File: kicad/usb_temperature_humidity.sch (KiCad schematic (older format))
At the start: 10 parts, among them SW1 SW_SPDT, SW2 SW_SPDT, U1 SeeeduinoXIAO, U2 SHT-31, U3 PinHeader_XIAO, U4 PinHeader_XIAO

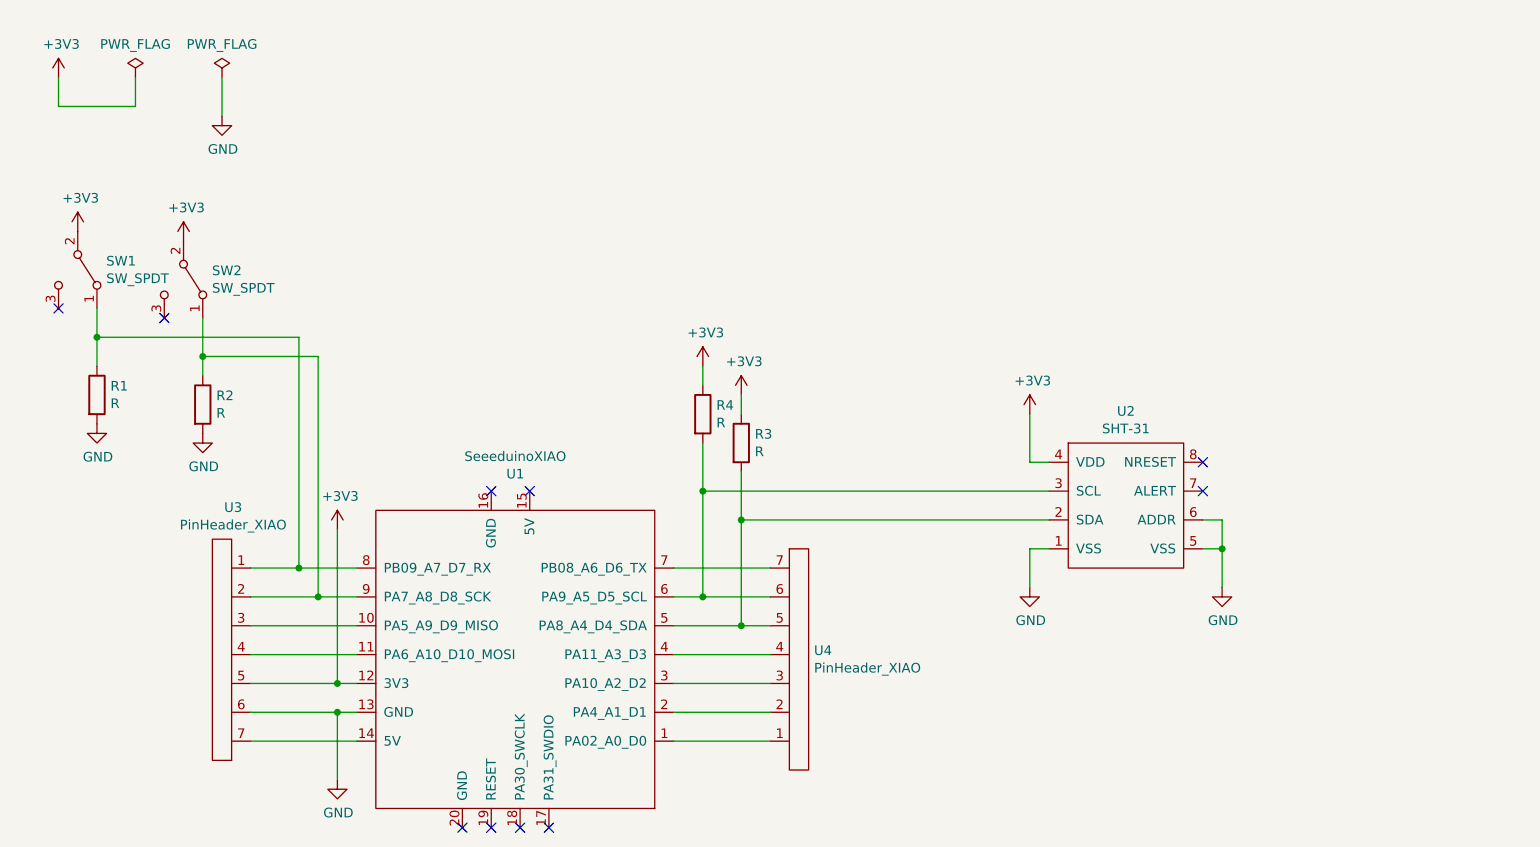
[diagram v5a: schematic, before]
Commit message: OPENジャンパを介してALERT,NRESETをXIAOに繋いだ
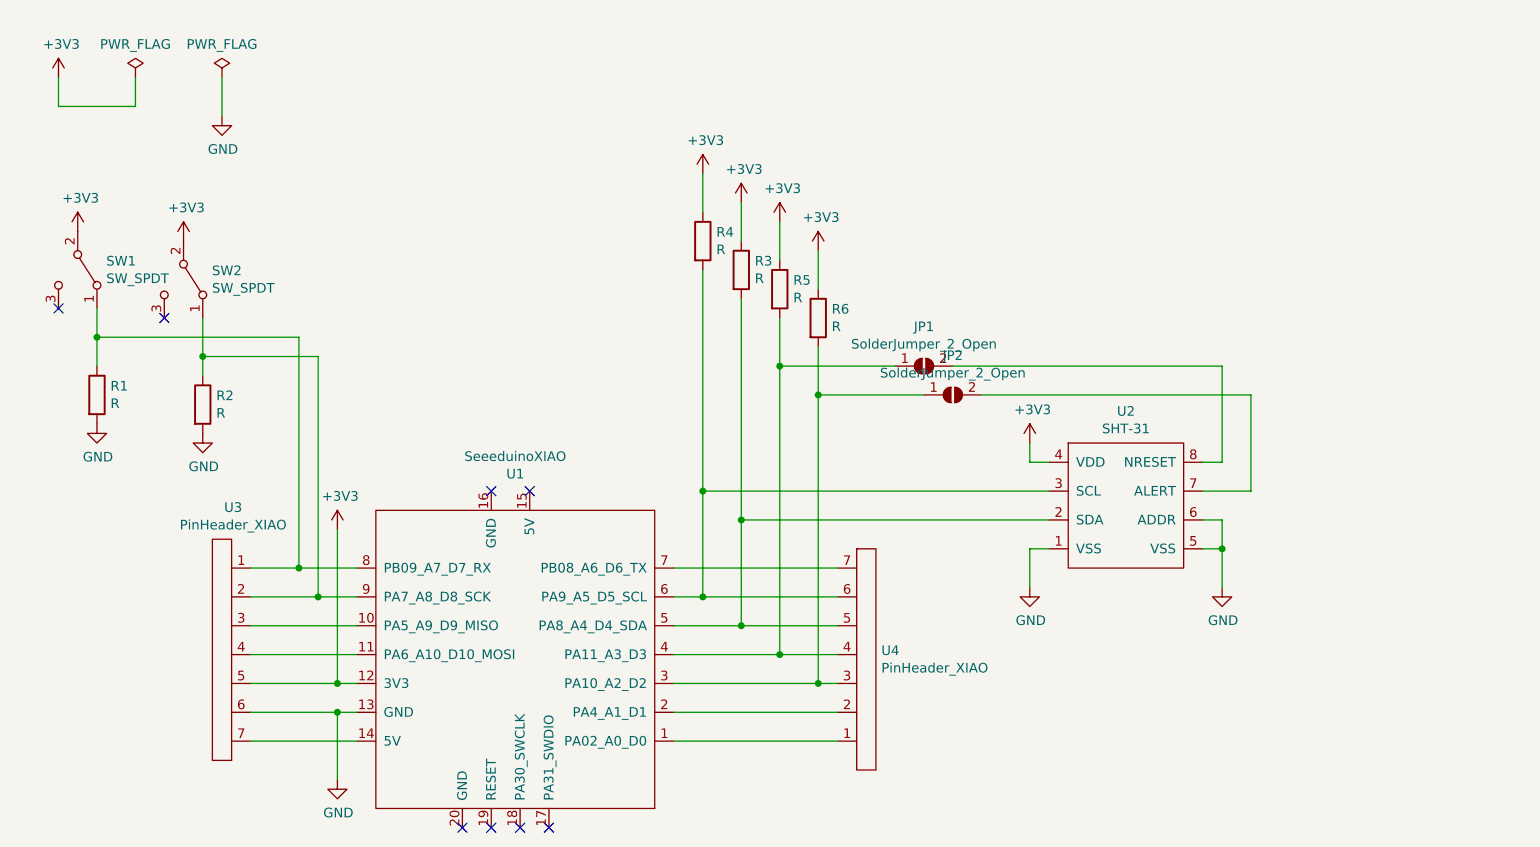
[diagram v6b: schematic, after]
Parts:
- added JP1, JP2: SolderJumper_2_Open, Jumper:SolderJumper-2_P1.3mm_Open_TrianglePad1.0x1.5mm, symbol Jumper:SolderJumper_2_Open
- added R5, R6: R, Resistor_THT:R_Axial_DIN0207_L6.3mm_D2.5mm_P10.16mm_Horizontal, symbol Device:R
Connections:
- net +3V3: now also R5.1, R6.1
- net at U1.3 (PA10_A2_D2), U4.3: now also JP2.1 (A), R6.2
- net at U1.4 (PA11_A3_D3), U4.4: now also JP1.1 (A), R5.2
- net at U2.7 (ALERT): now also JP2.2 (B)
- net at U2.8 (NRESET): now also JP1.2 (B)
- no-connect marks 10 -> 8
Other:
- moved on the sheet: R3, R4, U4
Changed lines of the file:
@@
 	900  1050 900  1200
-$Comp
-L power:+3V3 #PWR03
-U 1 1 5F4047C9
-P 2350 3400
-F 0 "#PWR03" H 2350 3250 50  0001 C CNN
-F 1 "+3V3" H 2365 3573 50  0000 C CNN
-F 2 "" H 2350 3400 50  0001 C CNN
-F 3 "" H 2350 3400 50  0001 C CNN
-	1    2350 3400
-	1    0    0    -1
-$EndComp
 $Comp
 L power:GND #PWR02
@@
 L Device:R R4
 U 1 1 5F3FC51D
-P 4250 2800
-F 0 "R4" H 4320 2846 50  0000 L CNN
-F 1 "R" H 4320 2755 50  0000 L CNN
-F 2 "Resistor_THT:R_Axial_DIN0207_L6.3mm_D2.5mm_P10.16mm_Horizontal" V 4180 2800 50  0001 C CNN
-F 3 "~" H 4250 2800 50  0001 C CNN
-	1    4250 2800
+P 4250 1900
+F 0 "R4" H 4320 1946 50  0000 L CNN
+F 1 "R" H 4320 1855 50  0000 L CNN
+F 2 "Resistor_THT:R_Axial_DIN0207_L6.3mm_D2.5mm_P10.16mm_Horizontal" V 4180 1900 50  0001 C CNN
+F 3 "~" H 4250 1900 50  0001 C CNN
+	1    4250 1900
 	1    0    0    -1
 $EndComp
@@
 L Device:R R3
 U 1 1 5F3FC106
-P 4450 2950
-F 0 "R3" H 4520 2996 50  0000 L CNN
-F 1 "R" H 4520 2905 50  0000 L CNN
-F 2 "Resistor_THT:R_Axial_DIN0207_L6.3mm_D2.5mm_P10.16mm_Horizontal" V 4380 2950 50  0001 C CNN
-F 3 "~" H 4450 2950 50  0001 C CNN
-	1    4450 2950
+P 4450 2050
+F 0 "R3" H 4520 2096 50  0000 L CNN
+F 1 "R" H 4520 2005 50  0000 L CNN
+F 2 "Resistor_THT:R_Axial_DIN0207_L6.3mm_D2.5mm_P10.16mm_Horizontal" V 4380 2050 50  0001 C CNN
+F 3 "~" H 4450 2050 50  0001 C CNN
+	1    4450 2050
 	1    0    0    -1
 $EndComp
@@
 $EndComp
 Wire Wire Line
-	4250 2950 4250 3200
-Wire Wire Line
-	4450 3100 4450 3350
-Wire Wire Line
 	6050 3200 4250 3200
-Connection ~ 4250 3200
-Wire Wire Line
-	4250 3200 4250 3750
 Wire Wire Line
 	6050 3350 4450 3350
-Connection ~ 4450 3350
 Wire Wire Line
 	4450 3350 4450 3900
@@
 Wire Wire Line
 	6050 3050 5950 3050
-Wire Wire Line
-	5950 3050 5950 2800
-NoConn ~ 6850 3050
-NoConn ~ 6850 3200
 NoConn ~ 3350 3200
 NoConn ~ 3150 3200
@@
 NoConn ~ 3150 4950
 NoConn ~ 3000 4950
-$Comp
-L power:+3V3 #PWR06
-U 1 1 5F3FB873
-P 4450 2700
-F 0 "#PWR06" H 4450 2550 50  0001 C CNN
-F 1 "+3V3" H 4465 2873 50  0000 C CNN
-F 2 "" H 4450 2700 50  0001 C CNN
-F 3 "" H 4450 2700 50  0001 C CNN
-	1    4450 2700
-	1    0    0    -1
-$EndComp
-$Comp
-L power:+3V3 #PWR05
-U 1 1 5F3FBC68
-P 4250 2550
-F 0 "#PWR05" H 4250 2400 50  0001 C CNN
-F 1 "+3V3" H 4265 2723 50  0000 C CNN
-F 2 "" H 4250 2550 50  0001 C CNN
-F 3 "" H 4250 2550 50  0001 C CNN
-	1    4250 2550
-	1    0    0    -1
-$EndComp
-Wire Wire Line
-	4250 2550 4250 2650
-Wire Wire Line
-	4450 2700 4450 2800
 Wire Wire Line
 	1750 1050 1750 1250
@@
 L power:+3V3 #PWR07
 U 1 1 5F40C82C
-P 5950 2800
-F 0 "#PWR07" H 5950 2650 50  0001 C CNN
-F 1 "+3V3" H 5965 2973 50  0000 C CNN
-F 2 "" H 5950 2800 50  0001 C CNN
-F 3 "" H 5950 2800 50  0001 C CNN
-	1    5950 2800
+P 5950 2950
+F 0 "#PWR07" H 5950 2800 50  0001 C CNN
+F 1 "+3V3" H 5965 3123 50  0000 C CNN
+F 2 "" H 5950 2950 50  0001 C CNN
+F 3 "" H 5950 2950 50  0001 C CNN
+	1    5950 2950
 	1    0    0    -1
 $EndComp
@@
 NoConn ~ 900  2250
 $Comp
-L kicad_mylib:SHT-31 U2
-U 1 1 5FB3D220
-P 6150 3600
-F 0 "U2" H 6450 4415 50  0000 C CNN
-F 1 "SHT-31" H 6450 4324 50  0000 C CNN
-F 2 "kicad_mylib:SHT-31" H 6700 4300 50  0001 C CNN
-F 3 "" H 6700 4300 50  0001 C CNN
-	1    6150 3600
-	1    0    0    -1
-$EndComp
-$Comp
 L power:GND #PWR013
 U 1 1 5FB42E84
@@
 L kicad_mylib:PinHeader_XIAO U4
 U 1 1 5FB5C045
-P 4700 4650
-F 0 "U4" H 4828 5271 50  0000 L CNN
-F 1 "PinHeader_XIAO" H 4828 5180 50  0000 L CNN
-F 2 "kicad_mylib:PinHeader_XIAO" H 4750 5900 50  0001 C CNN
-F 3 "" H 4750 5900 50  0001 C CNN
-	1    4700 4650
+P 5050 4650
+F 0 "U4" H 5178 5271 50  0000 L CNN
+F 1 "PinHeader_XIAO" H 5178 5180 50  0000 L CNN
+F 2 "kicad_mylib:PinHeader_XIAO" H 5100 5900 50  0001 C CNN
+F 3 "" H 5100 5900 50  0001 C CNN
+	1    5050 4650
 	1    0    0    -1
 $EndComp
@@
 	-1   0    0    1
 $EndComp
-Wire Wire Line
-	4600 4500 4100 4500
-Wire Wire Line
-	4600 4350 4100 4350
-Wire Wire Line
-	4600 4200 4100 4200
-Wire Wire Line
-	4100 4050 4600 4050
-Wire Wire Line
-	4600 3900 4450 3900
 Connection ~ 4450 3900
-Wire Wire Line
-	4600 3750 4250 3750
 Connection ~ 4250 3750
-Wire Wire Line
-	4100 3600 4600 3600
 Wire Wire Line
 	2150 3600 1900 3600
@@
 Wire Wire Line
 	1900 4500 2450 4500
+Wire Wire Line
+	4250 3750 4950 3750
+$Comp
+L Jumper:SolderJumper_2_Open JP1
+U 1 1 5FB82EA1
+P 5400 2550
+F 0 "JP1" H 5400 2755 50  0000 C CNN
+F 1 "SolderJumper_2_Open" H 5400 2664 50  0000 C CNN
+F 2 "Jumper:SolderJumper-2_P1.3mm_Open_TrianglePad1.0x1.5mm" H 5400 2550 50  0001 C CNN
+F 3 "~" H 5400 2550 50  0001 C CNN
+	1    5400 2550
+	1    0    0    -1
+$EndComp
+$Comp
+L Jumper:SolderJumper_2_Open JP2
+U 1 1 5FB83C68
+P 5550 2700
+F 0 "JP2" H 5550 2905 50  0000 C CNN
+F 1 "SolderJumper_2_Open" H 5550 2814 50  0000 C CNN
+F 2 "Jumper:SolderJumper-2_P1.3mm_Open_TrianglePad1.0x1.5mm" H 5550 2700 50  0001 C CNN
+F 3 "~" H 5550 2700 50  0001 C CNN
+	1    5550 2700
+	1    0    0    -1
+$EndComp
+Wire Wire Line
+	5950 2950 5950 3050
+Wire Wire Line
+	4100 4200 4850 4200
+$Comp
+L Device:R R6
+U 1 1 5FB80CC5
+P 4850 2300
+F 0 "R6" H 4920 2346 50  0000 L CNN
+F 1 "R" H 4920 2255 50  0000 L CNN
+F 2 "Resistor_THT:R_Axial_DIN0207_L6.3mm_D2.5mm_P10.16mm_Horizontal" V 4780 2300 50  0001 C CNN
+F 3 "~" H 4850 2300 50  0001 C CNN
+	1    4850 2300
+	1    0    0    -1
+$EndComp
+$Comp
+L Device:R R5
+U 1 1 5FB808DA
+P 4650 2150
+F 0 "R5" H 4720 2196 50  0000 L CNN
+F 1 "R" H 4720 2105 50  0000 L CNN
+F 2 "Resistor_THT:R_Axial_DIN0207_L6.3mm_D2.5mm_P10.16mm_Horizontal" V 4580 2150 50  0001 C CNN
+F 3 "~" H 4650 2150 50  0001 C CNN
+	1    4650 2150
+	1    0    0    -1
+$EndComp
+Wire Wire Line
+	5700 2700 7100 2700
+Wire Wire Line
+	6950 2550 5550 2550
+Wire Wire Line
+	4450 3900 4950 3900
+Connection ~ 4850 4200
+Wire Wire Line
+	4850 4200 4950 4200
+$Comp
+L kicad_mylib:SHT-31 U2
+U 1 1 5FB3D220
+P 6150 3600
+F 0 "U2" H 6450 4415 50  0000 C CNN
+F 1 "SHT-31" H 6450 4324 50  0000 C CNN
+F 2 "kicad_mylib:SHT-31" H 6700 4300 50  0001 C CNN
+F 3 "" H 6700 4300 50  0001 C CNN
+	1    6150 3600
+	1    0    0    -1
+$EndComp
+Wire Wire Line
+	7100 3200 6850 3200
+Wire Wire Line
+	6950 3050 6850 3050
+Wire Wire Line
+	4250 1550 4250 1750
+Wire Wire Line
+	4450 1700 4450 1900
+$Comp
+L power:+3V3 #PWR015
+U 1 1 5FB81892
+P 4850 1950
+F 0 "#PWR015" H 4850 1800 50  0001 C CNN
+F 1 "+3V3" H 4865 2123 50  0000 C CNN
+F 2 "" H 4850 1950 50  0001 C CNN
+F 3 "" H 4850 1950 50  0001 C CNN
+	1    4850 1950
+	1    0    0    -1
+$EndComp
+$Comp
+L power:+3V3 #PWR014
+U 1 1 5FB81400
+P 4650 1800
+F 0 "#PWR014" H 4650 1650 50  0001 C CNN
+F 1 "+3V3" H 4665 1973 50  0000 C CNN
+F 2 "" H 4650 1800 50  0001 C CNN
+F 3 "" H 4650 1800 50  0001 C CNN
+	1    4650 1800
+	1    0    0    -1
+$EndComp
+$Comp
+L power:+3V3 #PWR06
+U 1 1 5F3FB873
+P 4450 1700
+F 0 "#PWR06" H 4450 1550 50  0001 C CNN
+F 1 "+3V3" H 4465 1873 50  0000 C CNN
+F 2 "" H 4450 1700 50  0001 C CNN
+F 3 "" H 4450 1700 50  0001 C CNN
+	1    4450 1700
+	1    0    0    -1
+$EndComp
+$Comp
+L power:+3V3 #PWR05
+U 1 1 5F3FBC68
+P 4250 1550
+F 0 "#PWR05" H 4250 1400 50  0001 C CNN
+F 1 "+3V3" H 4265 1723 50  0000 C CNN
+F 2 "" H 4250 1550 50  0001 C CNN
+F 3 "" H 4250 1550 50  0001 C CNN
+	1    4250 1550
+	1    0    0    -1
+$EndComp
+Wire Wire Line
+	6950 2550 6950 3050
+Wire Wire Line
+	7100 2700 7100 3200
+Wire Wire Line
+	4100 4050 4650 4050
+Wire Wire Line
+	4100 3600 4950 3600
+Wire Wire Line
+	4650 2300 4650 2550
+Connection ~ 4650 4050
+Wire Wire Line
+	4650 4050 4950 4050
+Wire Wire Line
+	5250 2550 4650 2550
+Connection ~ 4650 2550
+Wire Wire Line
+	4450 2200 4450 3350
+Connection ~ 4450 3350
+Wire Wire Line
+	4250 2050 4250 3200
+Connection ~ 4250 3200
+Wire Wire Line
+	4250 3200 4250 3750
+Wire Wire Line
+	4850 1950 4850 2150
+Wire Wire Line
+	4650 1800 4650 2000
+Wire Wire Line
+	4100 4350 4950 4350
+Wire Wire Line
+	4100 4500 4950 4500
+Wire Wire Line
+	4650 2550 4650 4050
+Wire Wire Line
+	5400 2700 4850 2700
+Wire Wire Line
+	4850 2450 4850 2700
+Connection ~ 4850 2700
+Wire Wire Line
+	4850 2700 4850 4200
+$Comp
+L power:+3V3 #PWR03
+U 1 1 5F4047C9
+P 2350 3400
+F 0 "#PWR03" H 2350 3250 50  0001 C CNN
+F 1 "+3V3" H 2365 3573 50  0000 C CNN
+F 2 "" H 2350 3400 50  0001 C CNN
+F 3 "" H 2350 3400 50  0001 C CNN
+	1    2350 3400
+	1    0    0    -1
+$EndComp
 $EndSCHEMATC

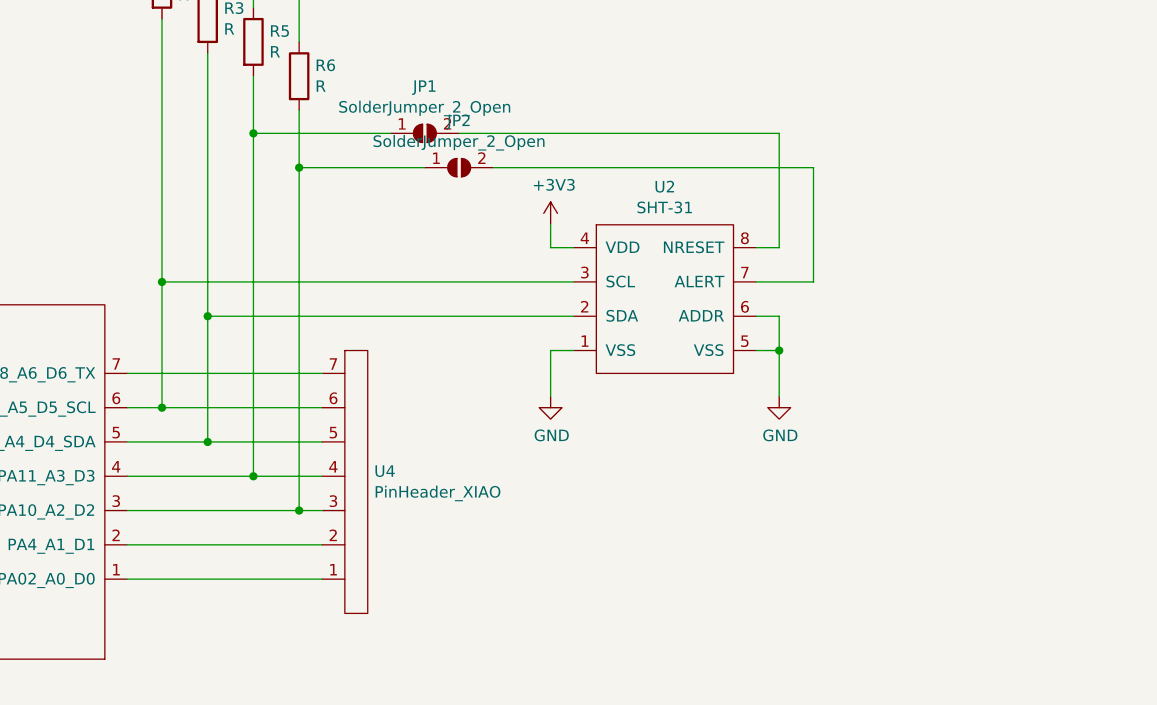
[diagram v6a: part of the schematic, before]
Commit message: aliexpress版のSHT-31をスキーマに追加した
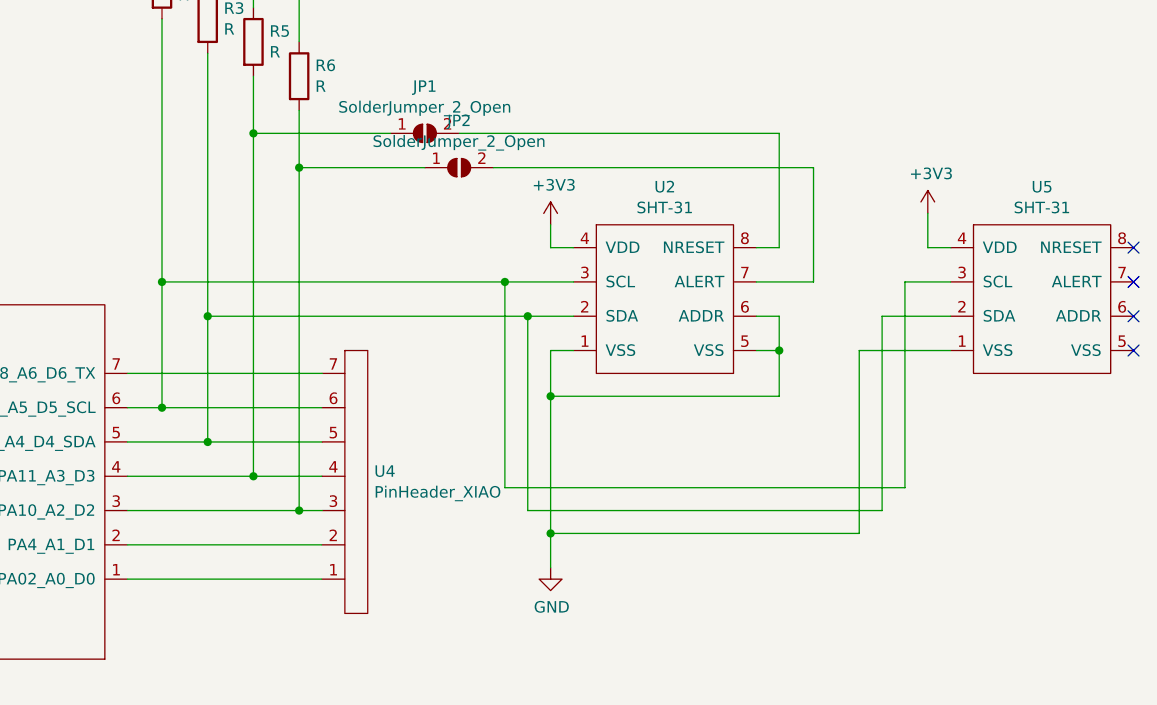
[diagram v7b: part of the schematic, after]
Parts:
- added U5: SHT-31, kicad_mylib:SHT-31_aliexpress, symbol kicad_mylib:SHT-31
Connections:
- net +3V3: now also U5.4 (VDD)
- net GND: now also U5.1 (VSS)
- net at R3.2, U1.5 (PA8_A4_D4_SDA), U2.2 (SDA)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: now also U5.2 (SDA)
- net at R4.2, U1.6 (PA9_A5_D5_SCL), U2.3 (SCL)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: now also U5.3 (SCL)
- no-connect marks 8 -> 12
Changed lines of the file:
@@
 L power:GND #PWR08
 U 1 1 5F40CEFE
-P 5950 3700
-F 0 "#PWR08" H 5950 3450 50  0001 C CNN
-F 1 "GND" H 5955 3527 50  0000 C CNN
-F 2 "" H 5950 3700 50  0001 C CNN
-F 3 "" H 5950 3700 50  0001 C CNN
-	1    5950 3700
+P 5950 4450
+F 0 "#PWR08" H 5950 4200 50  0001 C CNN
+F 1 "GND" H 5955 4277 50  0000 C CNN
+F 2 "" H 5950 4450 50  0001 C CNN
+F 3 "" H 5950 4450 50  0001 C CNN
+	1    5950 4450
 	1    0    0    -1
 $EndComp
@@
 $EndComp
 Wire Wire Line
-	6050 3200 4250 3200
-Wire Wire Line
-	6050 3350 4450 3350
+	6050 3200 5750 3200
+Wire Wire Line
+	6050 3350 5850 3350
 Wire Wire Line
 	4450 3350 4450 3900
@@
 NoConn ~ 1450 2300
 NoConn ~ 900  2250
-$Comp
-L power:GND #PWR013
-U 1 1 5FB42E84
-P 6950 3700
-F 0 "#PWR013" H 6950 3450 50  0001 C CNN
-F 1 "GND" H 6955 3527 50  0000 C CNN
-F 2 "" H 6950 3700 50  0001 C CNN
-F 3 "" H 6950 3700 50  0001 C CNN
-	1    6950 3700
-	1    0    0    -1
-$EndComp
 Wire Wire Line
 	6850 3350 6950 3350
@@
 Wire Wire Line
 	6850 3500 6950 3500
-Connection ~ 6950 3500
-Wire Wire Line
-	6950 3500 6950 3700
 $Comp
 L kicad_mylib:PinHeader_XIAO U4
@@
 	1    0    0    -1
 $EndComp
+$Comp
+L kicad_mylib:SHT-31 U5
+U 1 1 5FDA7FE4
+P 7800 3600
+F 0 "U5" H 8100 4415 50  0000 C CNN
+F 1 "SHT-31" H 8100 4324 50  0000 C CNN
+F 2 "kicad_mylib:SHT-31_aliexpress" H 8350 4300 50  0001 C CNN
+F 3 "" H 8350 4300 50  0001 C CNN
+	1    7800 3600
+	1    0    0    -1
+$EndComp
+Connection ~ 5950 4300
+Wire Wire Line
+	5950 4300 5950 4450
+Wire Wire Line
+	7700 3500 7300 3500
+Wire Wire Line
+	7300 3500 7300 4300
+Wire Wire Line
+	7700 3200 7500 3200
+Wire Wire Line
+	7500 4100 5750 4100
+Wire Wire Line
+	5750 4100 5750 3200
+Wire Wire Line
+	7500 3200 7500 4100
+Connection ~ 5750 3200
+Wire Wire Line
+	5750 3200 4250 3200
+Wire Wire Line
+	7700 3350 7400 3350
+Wire Wire Line
+	7400 3350 7400 4200
+Wire Wire Line
+	7400 4200 5850 4200
+Wire Wire Line
+	5850 4200 5850 3350
+Connection ~ 5850 3350
+Wire Wire Line
+	5850 3350 4450 3350
+$Comp
+L power:+3V3 #PWR013
+U 1 1 5FDBE277
+P 7600 2900
+F 0 "#PWR013" H 7600 2750 50  0001 C CNN
+F 1 "+3V3" H 7615 3073 50  0000 C CNN
+F 2 "" H 7600 2900 50  0001 C CNN
+F 3 "" H 7600 2900 50  0001 C CNN
+	1    7600 2900
+	1    0    0    -1
+$EndComp
+Wire Wire Line
+	7600 3050 7600 2900
+Wire Wire Line
+	7600 3050 7700 3050
+NoConn ~ 8500 3500
+NoConn ~ 8500 3350
+NoConn ~ 8500 3200
+NoConn ~ 8500 3050
+Wire Wire Line
+	7300 4300 5950 4300
+Wire Wire Line
+	6950 3500 6950 3700
+Wire Wire Line
+	6950 3700 5950 3700
+Connection ~ 6950 3500
+Connection ~ 5950 3700
+Wire Wire Line
+	5950 3700 5950 4300
 $EndSCHEMATC
